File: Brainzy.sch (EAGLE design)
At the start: 46 parts, among them IC1 L293D, IC2 L293D

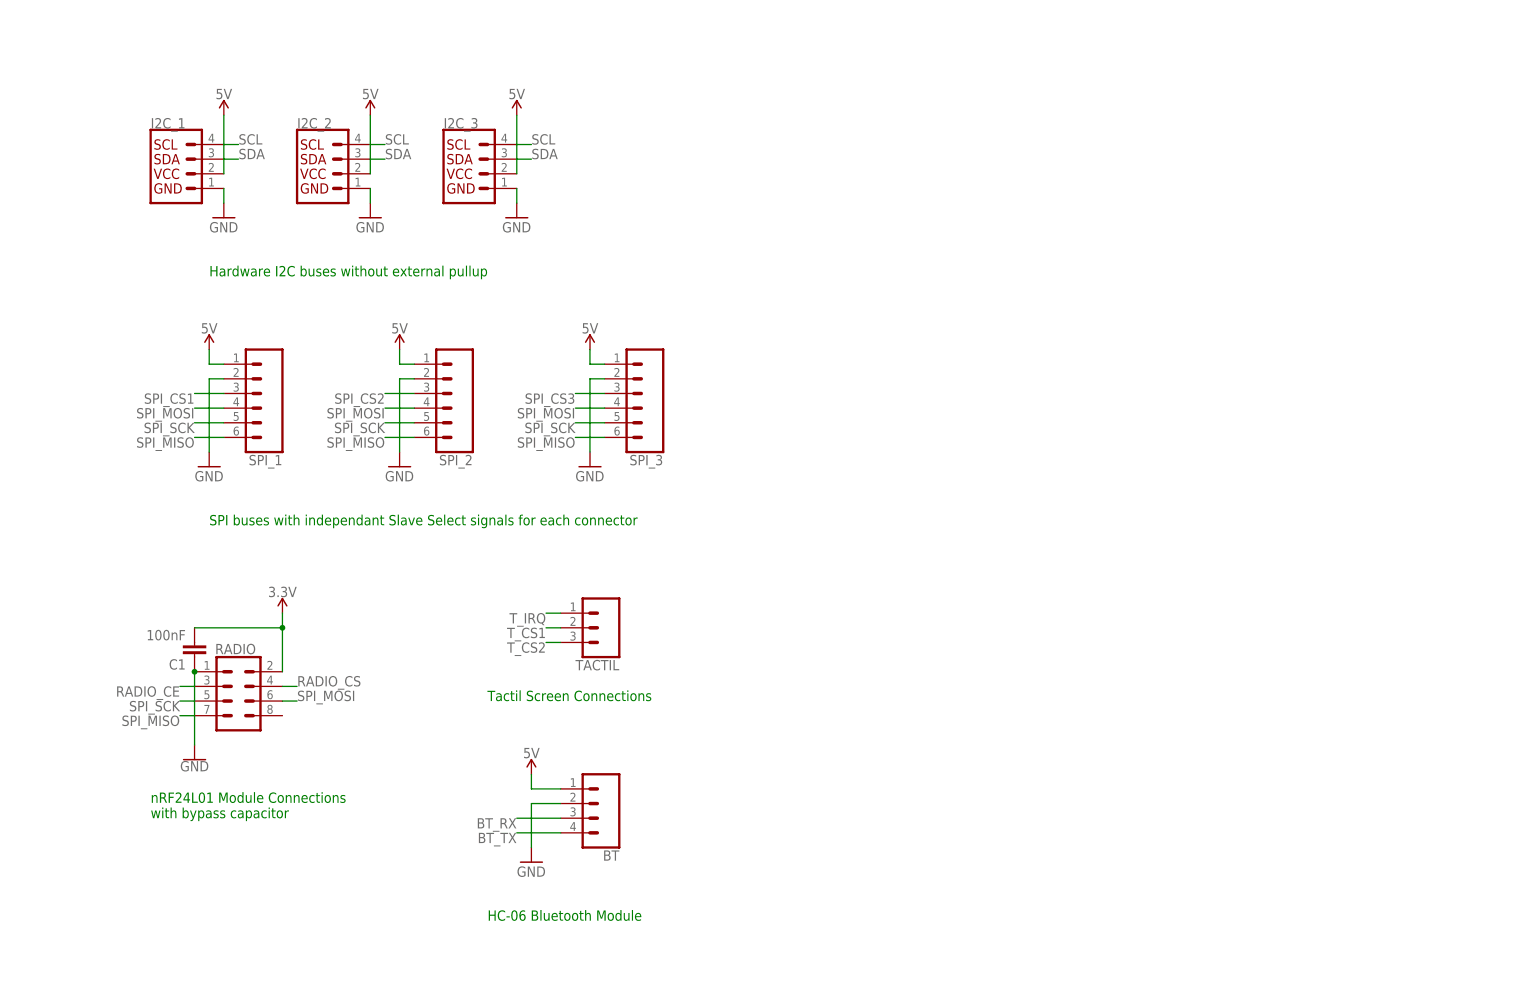
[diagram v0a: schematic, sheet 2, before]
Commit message: Upload Brainzy v1.1
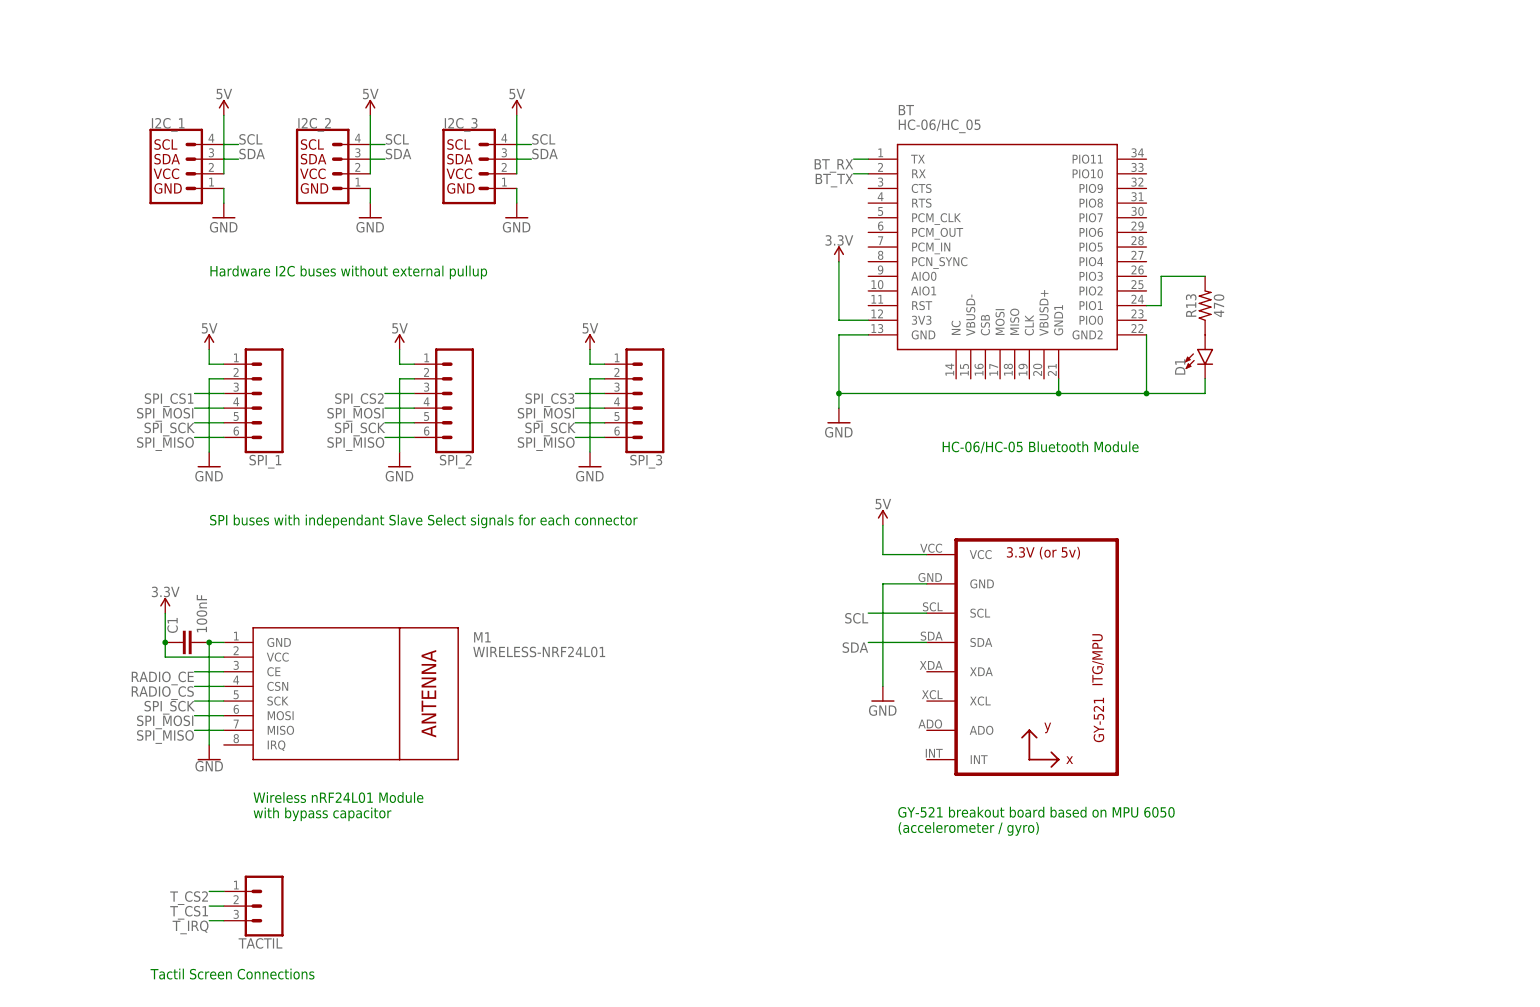
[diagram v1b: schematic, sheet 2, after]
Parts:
- removed IU, RADIO: (no value), SparkFun-Connectors:CONN_04X2
- removed U$1: DC-DC-STEP-DOWN-LM2596, DC-DC-STEP-DOWN-LM2596:DC-DC-STEP-DOWN-LM2596
- added D1: (no value), SparkFun-LED:LED1206
- added M1: WIRELESS-NRF24L01, diy-modules copy:WIRELESS-NRF24L01
- added POWER_CONVERTER: DC-DC-STEP-DOWN-LM2596, diy-modules copy:DC-DC-STEP-DOWN-LM2596
- added R13: 470, SparkFun-Resistors:10OHM-1206-1/4W-1%
- added U1: GY-521MPU6050, gy-521:GY-521MPU6050
- added USER_INTERFACE: (no value), SparkFun-Connectors:CONN_04X2
- BATT: value (none) -> 5.5x2.1mm Barrel; device SparkFun-Connectors:CONN_025MM -> SparkFun-Connectors:POWER_JACKSMD
- BT: value (none) -> HC-06/HC_05; device SparkFun-Connectors:CONN_04 -> SerialPortBluetooth:HC_05
- TEENSY_3.2/3.5: value TEENSY_3.5_ALL_PINS -> TEENSY_ALL_PINS
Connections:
- removed net N$2: IU.2, R1.1
- new net N$3: D1.A, R13.1
- new net N$4: R12.1, USER_INTERFACE.6
- new net N$6: BT.PIO1, R13.2
- net 12V: now also BATT.PWR, POWER_CONVERTER.IN+; no longer BATT.2, U$1.IN+
- net 3.3V: now also BT.3V3, C1.1, M1.VCC; no longer C1.2, RADIO.2
- net 5V: now also POWER_CONVERTER.OUT+, U1.VCC; no longer BT.1, U$1.OUT+
- net BTN_CENTER: now also USER_INTERFACE.3; no longer IU.8
- net BTN_DOWN: now also USER_INTERFACE.7; no longer IU.3
- net BTN_LEFT: now also USER_INTERFACE.2; no longer IU.6
- net BTN_RIGHT: now also USER_INTERFACE.5; no longer IU.5
- net BTN_UP: now also USER_INTERFACE.4; no longer IU.4
- net BT_RX: now also BT.TX; no longer BT.3
- net BT_TX: now also BT.RX; no longer BT.4
- net GND: now also BATT.GNDBREAK, BT.GND, BT.GND1, BT.GND2, C1.2, D1.C, M1.GND, POWER_CONVERTER.IN-, POWER_CONVERTER.OUT-, U1.GND, USER_INTERFACE.1; no longer BATT.1, BT.2, C1.1, IU.7, RADIO.1, U$1.IN-, U$1.OUT-
- net MOT1_1: now also TEENSY_3.2/3.5.21/A7/PWM; no longer TEENSY_3.2/3.5.23/A9/PWM
- net MOT1_2: now also TEENSY_3.2/3.5.20/A6/PWM; no longer TEENSY_3.2/3.5.22/A8/PWM
- net MOT2_1: now also TEENSY_3.2/3.5.23/A9/PWM; no longer TEENSY_3.2/3.5.21/A7/PWM
- net MOT2_2: now also TEENSY_3.2/3.5.22/A8/PWM; no longer TEENSY_3.2/3.5.20/A6/PWM
- net N$1: now also R1.1, USER_INTERFACE.8; no longer IU.1, R12.1
- net RADIO_CE: now also M1.CE, TEENSY_3.2/3.5.38/A19/SDA1/PWM; no longer RADIO.3, TEENSY_3.2/3.5.37/A18/SCL1/PWM
- net RADIO_CS: now also M1.CSN, TEENSY_3.2/3.5.37/A18/SCL1/PWM; no longer RADIO.4, TEENSY_3.2/3.5.38/A19/SDA1/PWM
- net SCL: now also U1.SCL
- net SDA: now also U1.SDA
- net SPI_MISO: now also M1.MISO; no longer RADIO.7
- net SPI_MOSI: now also M1.MOSI; no longer RADIO.6
- net SPI_SCK: now also M1.SCK; no longer RADIO.5
- net T_CS2: now also TACTIL.1; no longer TACTIL.3
- net T_IRQ: now also TACTIL.3; no longer TACTIL.1
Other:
- note added: "GY-521 breakout board based on MPU 6050 (accelerometer / gyro)"
- note added: "HC-06/HC-05 Bluetooth Module"
- note added: "Power Regulation"
- note added: "Wireless nRF24L01 Module with bypass capacitor"
- note removed: "HC-06 Bluetooth Module"
- note removed: "Power Regulation 5V"
- note removed: "nRF24L01 Module Connections with bypass capacitor"
- moved on the sheet: BATT, C1, R1, R12, RESET, TACTIL

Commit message: Upload Brainzy v2.0
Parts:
- removed BATT_CELL: (no value), SparkFun-Connectors:CONN_04POLAR
- removed BT: HC-06/HC_05, SerialPortBluetooth:HC_05
- removed I2C_1, I2C_2, I2C_3: (no value), SparkFun-Connectors:I2C_STANDARD
- removed IC1, IC2: L293D, st-microelectronics:L293D
- removed LS1: BUZZER-PTH, SparkFun-Electromechanical:BUZZER-PTH
- removed MOT_1, MOT_2, MOT_3, SPI_1, SPI_2, SPI_3: (no value), SparkFun-Connectors:CONN_06POLAR
- removed POWER_CONVERTER: DC-DC-STEP-DOWN-LM2596, diy-modules copy:DC-DC-STEP-DOWN-LM2596
- removed RESET: MOMENTARY-SWITCH-SPST-PTH-6.0MM, SparkFun-Switches:MOMENTARY-SWITCH-SPST-PTH-6.0MM
- removed SHARP_1, SHARP_2, SHARP_3, SHARP_4, SHARP_5, SHARP_6: (no value), SparkFun-Connectors:CONN_03
- removed TACTIL: (no value), SparkFun-Connectors:CONN_03POLAR
- removed TEENSY_3.2/3.5: TEENSY_ALL_PINS, Teensy_3_and_LC_Series_Boards_v1.4:TEENSY_3.5_ALL_PINS
- removed USER_INTERFACE: (no value), SparkFun-Connectors:CONN_04X2
- added BUZZER: (no value), MrRobotics-Components:BUZZER_MINI1X03_NO_SILK
- added D2: (no value), SparkFun-LED:LED-FKIT-1206
- added H1, H2, H3, H4: MOUNT-HOLE3.2, holes:MOUNT-HOLE3.2
- added I2C1, I2C2, I2C3: (no value), SparkFun-Connectors:CONN_04
- added J7: 5.5x2.1mm Barrel, SparkFun-Connectors:POWER_JACKSMD
- added JP1: JUMPER-SMT_2_NO_NO-SILK, SparkFun-Jumpers:JUMPER-SMT_2_NO_NO-SILK
- added MOT_FRONT, MOT_LEFT, MOT_RIGHT, SPI1, SPI2, SPI3: JST-XH-06-PIN-ROUND-PAD, MrRobotics-Connectors:JST-XH-06-PIN-ROUND-PAD
- added Q1, Q2, Q3: BSS138, MrRobotics-Transistors:BSS138
- added R14, R15, R16, R18, R21: 470k, SparkFun-Resistors:10OHM-1206-1/4W-1%
- added R17: 150k, SparkFun-Resistors:10OHM-1206-1/4W-1%
- added R19: 10k, SparkFun-Resistors:10OHM-1206-1/4W-1%
- added R20: 1k, SparkFun-Resistors:10OHM-1206-1/4W-1%
- added S1, S3: (no value), SparkFun-Switches:MOMENTARY-SWITCH-SPST-2-SMD-5.2MM
- added S2: (no value), SparkFun-Switches:SWITCH-SPDT-SMD-RIGHT-ANGLE
- added SHARP1, SHARP2, SHARP3, SHARP4, SHARP5, SHARP6: (no value), SparkFun-Connectors:CONN_03
- added T1, T2, T3: BSS84, MrRobotics-Transistors:BSS84
- added T4: S12323DS, MrRobotics-Transistors:S12323DS
- added TOUCH: JST-XH-02-PIN-ROUND-PAD, MrRobotics-Connectors:JST-XH-02-PIN-ROUND-PAD
- added U$1: TEENSY_3.5-3.2INV, MrRobotics-Boards:TEENSY_3.5-3.2INV
- added U$2: DC-DC-STEP-DOWN-MP2307_SMD, MrRobotics-Modules:DC-DC-STEP-DOWN-MP2307_SMD
- added U$3: LOGO, MrRobotics-Aesthetics:LOGO
- added U$4: LOGO_FR, MrRobotics-Aesthetics:LOGO_FR
- added U2: L293DD, MrRobotics-Components:L293DD
- added U3: HC_05, MrRobotics-Components:HC_05
- added U4: GY-521MPU6050, MrRobotics-Modules:GY-521MPU6050
- added UI: (no value), SparkFun-Connectors:CONN_04X2
- BATT: value 5.5x2.1mm Barrel -> JST-XH-04-PIN-ROUND-PAD; device SparkFun-Connectors:POWER_JACKSMD -> MrRobotics-Connectors:JST-XH-04-PIN-ROUND-PAD
- C1: value 100nF -> 10uF; device SparkFun-Capacitors:1.0UF-1206-50V-10% -> SparkFun-Capacitors:10UF-1206-6.3V-20%
- C7: value 10uF -> 100nF
- D1: device SparkFun-LED:LED1206 -> SparkFun-LED:LED-FKIT-1206
- M1: device diy-modules copy:WIRELESS-NRF24L01 -> MrRobotics-Modules:WIRELESS-NRF24L01
- R11, R9: value 150k -> 470k
- R12: value 1k -> 470k
- R13: value 470 -> 150k
- R7: value 1k -> 750
- U1: value GY-521MPU6050 -> L293DD; device gy-521:GY-521MPU6050 -> MrRobotics-Components:L293DD
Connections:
- removed net BTN_RST: RESET.2, TEENSY_3.2/3.5.RESET
- removed net CELL1: BATT_CELL.2, TEENSY_3.2/3.5.A22/DAC1
- removed net CELL2: R10.1, R11.2, TEENSY_3.2/3.5.A21/DAC0
- removed net CELL3: R8.1, R9.2, TEENSY_3.2/3.5.39/A20
- removed net COD1_A: MOT_1.2, R2.1, TEENSY_3.2/3.5.15/A1
- removed net COD1_B: MOT_1.1, R3.1, TEENSY_3.2/3.5.14/A0/PWM
- removed net COD2_A: MOT_2.2, R4.1, TEENSY_3.2/3.5.17/A3/PWM
- removed net COD2_B: MOT_2.1, R5.1, TEENSY_3.2/3.5.16/A2
- removed net COD3_A: MOT_3.2, R6.1, TEENSY_3.2/3.5.28
- removed net COD3_B: MOT_3.1, R7.1, TEENSY_3.2/3.5.27
- removed net N$3: D1.A, R13.1
- removed net RADIO_CE: M1.CE, TEENSY_3.2/3.5.38/A19/SDA1/PWM
- removed net RADIO_CS: M1.CSN, TEENSY_3.2/3.5.37/A18/SCL1/PWM
- removed net SCL: I2C_1.4, I2C_2.4, I2C_3.4, TEENSY_3.2/3.5.19/A5/SCL0, U1.SCL
- removed net SDA: I2C_1.3, I2C_2.3, I2C_3.3, TEENSY_3.2/3.5.18/A4/SDA0, U1.SDA
- removed net T_CS1: TACTIL.2, TEENSY_3.2/3.5.25
- removed net T_CS2: TACTIL.1, TEENSY_3.2/3.5.26
- removed net VDD: BATT_CELL.4, R1.2, R8.2
- new net BATT1: T1.D, U$1.39/A20
- new net BATT2: R12.1, R13.2, U$1.A21/DAC0
- new net BATT3: R16.1, R17.2, U$1.A22/DAC1
- new net DTR: U3.PIO9
- new net ENC1_A: MOT_LEFT.5, R1.1, U$1.16/A2
- new net ENC1_B: MOT_LEFT.6, R2.1, U$1.17/A3/PWM
- new net ENC2_A: MOT_RIGHT.5, R3.1, U$1.8/TX3/PWM
- new net ENC2_B: MOT_RIGHT.6, R4.1, U$1.14/A0/PWM
- new net ENC3_A: MOT_FRONT.5, R5.1, U$1.27
- new net ENC3_B: MOT_FRONT.6, R6.1, U$1.28
- new net I2C_SCL: I2C1.4, I2C2.4, I2C3.4, U$1.19/A5/SCL0, U4.SCL
- new net I2C_SDA: I2C1.3, I2C2.3, I2C3.3, U$1.18/A4/SDA0, U4.SDA
- new net MPU_INT: U$1.26, U4.INT
- new net N$10: D1.A, R7.2
- new net N$11: Q2.D, R10.1
- new net N$12: S3.1, S3.2, U$1.PGM
- new net N$13: R14.2, R15.1, T3.G
- new net N$14: Q3.D, R14.1
- new net N$15: J7.PWR, R21.1, T4.S
- new net N$16: R21.2, S2.O, T4.G
- new net N$17: JP1.1, U4.ADO
- new net N$18: R19.1, S1.1, U3.PIO11, U3.PIO3
- new net N$2: D2.A, R20.1
- new net N$7: R10.2, R11.1, T2.G
- new net N$9: R7.1, U3.PIO1, U3.PIO8
- new net RF_CE: M1.CE, U$1.29/PWM
- new net RF_CS: M1.CSN, U$1.30/PWM
- new net S1: BATT.2, R9.2, T1.S
- new net S2: BATT.3, R11.2, T2.S
- new net S3: BATT.4, R15.2, T3.S
- new net T_CS: TOUCH.1, U$1.25
- net 12V: now also R20.2, T4.D, U$2.IN+, U1.VS, U2.VS; no longer BATT.PWR, IC1.VCC2, IC2.VCC2, POWER_CONVERTER.IN+, R12.2
- net 3.3V: now also C7.2, Q1.G, Q2.G, Q3.G, R18.2, S1.3, U$1.3.3V, U3.3V3; no longer BT.3V3, C1.1, TEENSY_3.2/3.5.3.3V
- net 5V: now also C1.1, I2C1.2, I2C2.2, I2C3.2, JP1.2, MOT_FRONT.3, MOT_LEFT.3, MOT_RIGHT.3, R1.2, SHARP1.3, SHARP2.3, SHARP3.3, SHARP4.3, SHARP5.3, SHARP6.3, SPI1.6, SPI2.6, SPI3.6, U$1.VIN, U$2.OUT+, U1.EN1, U1.EN2, U1.VSS, U2.EN2, U2.VSS, U4.VCC, UI.2; no longer C7.1, I2C_1.2, I2C_2.2, I2C_3.2, IC1.1-2EN, IC1.3-4EN, IC1.VCC1, IC2.1-2EN, IC2.VCC1, MOT_1.4, MOT_2.4, MOT_3.4, POWER_CONVERTER.OUT+, R7.2, SHARP_1.3, SHARP_2.3, SHARP_3.3, SHARP_4.3, SHARP_5.3, SHARP_6.3, SPI_1.1, SPI_2.1, SPI_3.1, TEENSY_3.2/3.5.VIN, U1.VCC
- net BTN_CENTER: now also U$1.4/CAN0-RX/SDA2/PWM, UI.5; no longer TEENSY_3.2/3.5.4/CAN0-RX/SDA2/PWM, USER_INTERFACE.3
- net BTN_DOWN: now also U$1.7/RX3/PWM, UI.4; no longer TEENSY_3.2/3.5.6/PWM, USER_INTERFACE.7
- net BTN_LEFT: now also U$1.3/CAN0-TX/SCL2/PWM, UI.3; no longer TEENSY_3.2/3.5.3/CAN0-TX/SCL2/PWM, USER_INTERFACE.2
- net BTN_RIGHT: now also U$1.5/PWM, UI.6; no longer TEENSY_3.2/3.5.5/PWM, USER_INTERFACE.5
- net BTN_UP: now also U$1.2/PWM, UI.1; no longer TEENSY_3.2/3.5.2/PWM, USER_INTERFACE.4
- net BT_RX: now also U$1.0/RX1/MOSI1, U3.TX; no longer BT.TX, TEENSY_3.2/3.5.0/RX1/MOSI1
- net BT_TX: now also U$1.1/TX1/MISO1, U3.RX; no longer BT.RX, TEENSY_3.2/3.5.1/TX1/MISO1
- net BUZZER: now also BUZZER.1, U$1.6/PWM; no longer LS1.2, TEENSY_3.2/3.5.7/RX3/PWM
- net GND: now also BATT.1, BUZZER.3, C7.1, D2.C, I2C1.1, I2C2.1, I2C3.1, J7.GND, J7.GNDBREAK, MOT_FRONT.4, MOT_LEFT.4, MOT_RIGHT.4, Q1.S, Q2.S, Q3.S, R13.1, R17.1, R18.1, R19.2, S2.P, S2.S, S3.3, S3.4, SHARP1.2, SHARP2.2, SHARP3.2, SHARP4.2, SHARP5.2, SHARP6.2, SPI1.1, SPI2.1, SPI3.1, U$1.AGND, U$1.GND, U$2.IN-, U$2.OUT-, U1.GND@1, U1.GND@2, U1.GND@3, U1.GND@4, U1.GND@5, U1.GND@6, U1.GND@7, U1.GND@8, U2.EN1, U2.GND@1, U2.GND@2, U2.GND@3, U2.GND@4, U2.GND@5, U2.GND@6, U2.GND@7, U2.GND@8, U2.IN1, U2.IN2, U3.GND, U3.GND1, U3.GND2, U4.GND, UI.7, UI.8; no longer BATT.GNDBREAK, BATT_CELL.1, BT.GND, BT.GND1, BT.GND2, C7.2, I2C_1.1, I2C_2.1, I2C_3.1, IC1.GND1, IC1.GND2, IC1.GND3, IC1.GND4, IC2.3-4EN, IC2.GND1, IC2.GND2, IC2.GND3, IC2.GND4, LS1.1, MOT_1.3, MOT_2.3, MOT_3.3, POWER_CONVERTER.IN-, POWER_CONVERTER.OUT-, R11.1, R9.1, RESET.1, SHARP_1.2, SHARP_2.2, SHARP_3.2, SHARP_4.2, SHARP_5.2, SHARP_6.2, SPI_1.2, SPI_2.2, SPI_3.2, TEENSY_3.2/3.5.GND, U1.GND, USER_INTERFACE.1
- net MOT1_1: now also U$1.23/A9/PWM, U1.IN2; no longer IC1.1A, TEENSY_3.2/3.5.21/A7/PWM
- net MOT1_2: now also U$1.22/A8/PWM, U1.IN1; no longer IC1.2A, TEENSY_3.2/3.5.20/A6/PWM
- net MOT1_OUT1: now also MOT_LEFT.1, U1.OUT2; no longer IC1.1Y, MOT_1.6
- net MOT1_OUT2: now also MOT_LEFT.2, U1.OUT1; no longer IC1.2Y, MOT_1.5
- net MOT2_1: now also U$1.21/A7/PWM, U1.IN3; no longer IC1.3A, TEENSY_3.2/3.5.23/A9/PWM
- net MOT2_2: now also U$1.20/A6/PWM, U1.IN4; no longer IC1.4A, TEENSY_3.2/3.5.22/A8/PWM
- net MOT2_OUT1: now also MOT_RIGHT.1, U1.OUT3; no longer IC1.3Y, MOT_2.6
- net MOT2_OUT2: now also MOT_RIGHT.2, U1.OUT4; no longer IC1.4Y, MOT_2.5
- net MOT3_1: now also U$1.38/A19/SDA1/PWM, U2.IN3; no longer IC2.1A, TEENSY_3.2/3.5.30/PWM
- net MOT3_2: now also U$1.37/A18/SCL1/PWM, U2.IN4; no longer IC2.2A, TEENSY_3.2/3.5.29/PWM
- net MOT3_OUT1: now also MOT_FRONT.1, U2.OUT3; no longer IC2.1Y, MOT_3.6
- net MOT3_OUT2: now also MOT_FRONT.2, U2.OUT4; no longer IC2.2Y, MOT_3.5
- net N$1: now also R12.2, T2.D; no longer R1.1, USER_INTERFACE.8
- net N$4: now also R8.2, R9.1, T1.G; no longer R12.1, USER_INTERFACE.6
- net N$5: now also Q1.D, R8.1; no longer BATT_CELL.3, R10.2
- net N$6: now also R16.2, T3.D; no longer BT.PIO1, R13.2
- net SHARP1: now also SHARP1.1, U$1.33/A14/TX5; no longer SHARP_1.1, TEENSY_3.2/3.5.33/A14/TX5
- net SHARP2: now also SHARP2.1, U$1.34/A15/RX5; no longer SHARP_2.1, TEENSY_3.2/3.5.34/A15/RX5
- net SHARP3: now also SHARP3.1, U$1.35/A16/PWM; no longer SHARP_3.1, TEENSY_3.2/3.5.35/A16/PWM
- net SHARP4: now also SHARP4.1, U$1.36/A17/PWM; no longer SHARP_4.1, TEENSY_3.2/3.5.36/A17/PWM
- net SHARP5: now also SHARP5.1, U$1.32/A13/TX4/SCK1; no longer SHARP_5.1, TEENSY_3.2/3.5.32/A13/TX4/SCK1
- net SHARP6: now also SHARP6.1, U$1.31/A12/RX4; no longer SHARP_6.1, TEENSY_3.2/3.5.31/A12/RX4
- net SPI_CS1: now also SPI1.5, U$1.15/A1; no longer SPI_1.3, TEENSY_3.2/3.5.8/TX3/PWM
- net SPI_CS2: now also SPI2.5, U$1.9/RX2/PWM; no longer SPI_2.3, TEENSY_3.2/3.5.9/RX2/PWM
- net SPI_CS3: now also SPI3.5, U$1.10/TX2/PWM; no longer SPI_3.3, TEENSY_3.2/3.5.10/TX2/PWM
- net SPI_MISO: now also SPI1.2, SPI2.2, SPI3.2, U$1.12/MISO0; no longer SPI_1.6, SPI_2.6, SPI_3.6, TEENSY_3.2/3.5.12/MISO0
- net SPI_MOSI: now also SPI1.4, SPI2.4, SPI3.4, U$1.11/MOSI0; no longer SPI_1.4, SPI_2.4, SPI_3.4, TEENSY_3.2/3.5.11/MOSI0
- net SPI_SCK: now also SPI1.3, SPI2.3, SPI3.3, U$1.13/SCK0/LED; no longer SPI_1.5, SPI_2.5, SPI_3.5, TEENSY_3.2/3.5.13/SCK0/LED
- net T_IRQ: now also TOUCH.2, U$1.24; no longer TACTIL.3, TEENSY_3.2/3.5.24
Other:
- note added: "Communications I2C/SPI"
- note added: "HC-05 or HC-06 module can be used"
- note added: "IR Range Sensor"
- note added: "JP1 selects between I2C address 0x68 and 0x69"
- note added: "Motor Drivers"
- note added: "Power Control"
- note added: "Radio Communications"
- note added: "Teensy 3.2 or 3.5 can be used Only the Teensy 3.5 offers the total shield capacity"
- note removed: "Battery Connections"
- note removed: "Double H bridges"
- note removed: "GY-521 breakout board based on MPU 6050 (accelerometer / gyro)"
- note removed: "HC-06/HC-05 Bluetooth Module"
- note removed: "Hardware I2C buses without external pullup"
- note removed: "Motor Connections"
- note removed: "Power Regulation"
- note removed: "SHARP Connections"
- note removed: "SPI buses with independant Slave Select signals for each connector"
- note removed: "Tactil Screen Connections"
- note removed: "Teensy 3.2/3.5 Connections"
- note removed: "User interface"
- note removed: "Wireless nRF24L01 Module with bypass capacitor"
- note removed: "with bypass capacitors to remove electrical noise introduiced by SHARP sensors"

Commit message: Upload Brainzy v2.1
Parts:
- removed C5, C6: 10uF, SparkFun-Capacitors:10UF-1206-6.3V-20%
- removed C7: 100nF, SparkFun-Capacitors:10UF-1206-6.3V-20%
- removed M1: WIRELESS-NRF24L01, MrRobotics-Modules:WIRELESS-NRF24L01
- removed SHARP5, SHARP6: (no value), SparkFun-Connectors:CONN_03
- removed SPI1, SPI2, SPI3: JST-XH-06-PIN-ROUND-PAD, MrRobotics-Connectors:JST-XH-06-PIN-ROUND-PAD
- removed TOUCH: JST-XH-02-PIN-ROUND-PAD, MrRobotics-Connectors:JST-XH-02-PIN-ROUND-PAD
- added EXT_BT: (no value), SparkFun-Connectors:CONN_041X04_NO_SILK
- added Q4: BSS138, MrRobotics-Transistors:BSS138
- added R22: 10k, SparkFun-Resistors:10OHM-1206-1/4W-1%
- added R23, R25: 470k, SparkFun-Resistors:10OHM-1206-1/4W-1%
- added R24: 150k, SparkFun-Resistors:10OHM-1206-1/4W-1%
- added SPI: (no value), MrRobotics-Connectors:CONN_05X2_EXTSHD_LOCK
- added U$6: WIRELESS-WIFI-ESP-01, MrRobotics-Modules:WIRELESS-WIFI-ESP-01
- added UART: (no value), SparkFun-Connectors:CONN_04
- BATT: value JST-XH-04-PIN-ROUND-PAD -> BATTERY-CONNECTOR-LONG-PAD; device MrRobotics-Connectors:JST-XH-04-PIN-ROUND-PAD -> MrRobotics-Connectors:BATTERY-CONNECTOR-LONG-PAD
- MOT_FRONT, MOT_LEFT, MOT_RIGHT: value JST-XH-06-PIN-ROUND-PAD -> (none); device MrRobotics-Connectors:JST-XH-06-PIN-ROUND-PAD -> MrRobotics-Connectors:DC-MOTOR-CONNECTOR
- T4: value S12323DS -> SI2323DS; device MrRobotics-Transistors:S12323DS -> MrRobotics-Transistors:SI2323DS
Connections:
- removed net BUZZER: BUZZER.1, U$1.6/PWM
- removed net RF_CE: M1.CE, U$1.29/PWM
- removed net RF_CS: M1.CSN, U$1.30/PWM
- removed net SHARP5: SHARP5.1, U$1.32/A13/TX4/SCK1
- removed net SHARP6: SHARP6.1, U$1.31/A12/RX4
- new net BT_RST: S3.1, U3.RST
- new net EXT_RX: U$1.31/A12/RX4, UART.3
- new net EXT_TX: U$1.32/A13/TX4/SCK1, UART.4
- new net N$19: R23.2, T1.D
- new net N$20: BUZZER.3, Q4.D
- new net N$3: R22.1, U$6.CH_PD
- new net N$8: Q4.G, R25.1, U$1.6/PWM
- new net WIFI_RX: U$1.34/A15/RX5, U$6.UTXD
- new net WIFI_TX: U$1.33/A14/TX5, U$6.URXD
- net 3.3V: now also BUZZER.1, R22.2, U$6.VCC; no longer C7.2, M1.VCC
- net 5V: now also EXT_BT.1, MOT_FRONT.3-VCC, MOT_LEFT.3-VCC, MOT_RIGHT.3-VCC, SPI.1-VCC, UART.2; no longer C5.1, C6.1, MOT_FRONT.3, MOT_LEFT.3, MOT_RIGHT.3, SHARP5.3, SHARP6.3, SPI1.6, SPI2.6, SPI3.6
- net BATT1: now also R23.1, R24.2; no longer T1.D
- net BT_RX: now also EXT_BT.3
- net BT_TX: now also EXT_BT.4
- net ENC1_A: now also MOT_LEFT.5-CHA, R2.1; no longer MOT_LEFT.5, R1.1
- net ENC1_B: no longer MOT_LEFT.6, R2.1
- net ENC2_A: now also MOT_RIGHT.5-CHA, R4.1; no longer MOT_RIGHT.5, R3.1
- net ENC2_B: now also MOT_LEFT.6-CHB, MOT_RIGHT.6-CHB, R1.1, R3.1; no longer MOT_RIGHT.6, R4.1
- net ENC3_A: now also MOT_FRONT.5-CHA, R6.1; no longer MOT_FRONT.5, R5.1
- net ENC3_B: now also MOT_FRONT.6-CHB, R5.1; no longer MOT_FRONT.6, R6.1
- net GND: now also BATT.1-GND, EXT_BT.2, MOT_FRONT.4-GND, MOT_LEFT.4-GND, MOT_RIGHT.4-GND, Q4.S, R24.1, R25.2, SPI.2-GND, U$6.GND, UART.1; no longer BATT.1, BUZZER.3, C5.2, C6.2, C7.1, M1.GND, MOT_FRONT.4, MOT_LEFT.4, MOT_RIGHT.4, SHARP5.2, SHARP6.2, SPI1.1, SPI2.1, SPI3.1, UI.7
- net MOT1_OUT1: now also MOT_LEFT.1-M-; no longer MOT_LEFT.1
- net MOT1_OUT2: now also MOT_LEFT.2-M+; no longer MOT_LEFT.2
- net MOT2_OUT1: now also MOT_RIGHT.1-M-; no longer MOT_RIGHT.1
- net MOT2_OUT2: now also MOT_RIGHT.2-M+; no longer MOT_RIGHT.2
- net MOT3_1: now also U$1.29/PWM; no longer U$1.38/A19/SDA1/PWM
- net MOT3_2: now also U$1.30/PWM; no longer U$1.37/A18/SCL1/PWM
- net MOT3_OUT1: now also MOT_FRONT.1-M-; no longer MOT_FRONT.1
- net MOT3_OUT2: now also MOT_FRONT.2-M+; no longer MOT_FRONT.2
- net N$12: no longer S3.1
- net S1: now also BATT.2-S1; no longer BATT.2
- net S2: now also BATT.3-S2; no longer BATT.3
- net S3: now also BATT.4-S3; no longer BATT.4
- net SHARP1: now also U$1.38/A19/SDA1/PWM; no longer U$1.33/A14/TX5
- net SHARP2: now also U$1.37/A18/SCL1/PWM; no longer U$1.34/A15/RX5
- net SPI_CS1: now also SPI.4-CS1; no longer SPI1.5
- net SPI_CS2: now also SPI.6-CS2; no longer SPI2.5
- net SPI_CS3: now also SPI.8-CS3; no longer SPI3.5
- net SPI_MISO: now also SPI.7-MISO; no longer M1.MISO, SPI1.2, SPI2.2, SPI3.2
- net SPI_MOSI: now also SPI.5-MOSI; no longer M1.MOSI, SPI1.4, SPI2.4, SPI3.4
- net SPI_SCK: now also SPI.3-SCLK; no longer M1.SCK, SPI1.3, SPI2.3, SPI3.3
- net T_CS: now also SPI.9-T_CS; no longer TOUCH.1
- net T_IRQ: now also SPI.10-T_IRQ; no longer TOUCH.2
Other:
- note added: "Extension for HC-05/06 breakout board"
- note added: "I2C, SPI & UART Communications"
- note added: "IR Range Sensors"
- note added: "JP1 selects between I2C addresses 0x68 and 0x69"
- note added: "Wifi & Bluetooth Communications"
- note removed: "Communications I2C/SPI"
- note removed: "IR Range Sensor"
- note removed: "JP1 selects between I2C address 0x68 and 0x69"
- note removed: "Radio Communications"
- moved on the sheet: BUZZER, C1, C2, C3, C4, D1, D2, I2C1, I2C2, I2C3, J7, Q1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
